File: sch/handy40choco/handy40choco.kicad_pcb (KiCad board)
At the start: 2 copper layers, 169 x 71 mm, 95 parts, among them J1 Conn_01x20, SW1 SW_Push, SW10 SW_Push, SW11 SW_Push, SW12 SW_Push, SW13 SW_Push, SW14 SW_Push, SW15 SW_Push, SW16 SW_Push, SW17 SW_Push, SW18 SW_Push, SW19 SW_Push, SW2 SW_Push, SW20 SW_Push, SW21 SW_Push, SW22 SW_Push, SW23 SW_Push, SW24 SW_Push, SW25 SW_Push, SW26 SW_Push, SW27 SW_Push, SW28 SW_Push, SW29 SW_Push, SW3 SW_Push, SW30 SW_Push, SW31 SW_Push, SW32 SW_Push, SW33 SW_Push, SW34 SW_Push, SW35 SW_Push, SW36 SW_Push, SW37 SW_Push, SW38 SW_Push, SW39 SW_Push, SW4 SW_Push, SW40 SW_Push, SW5 SW_Push, SW6 SW_Push, SW7 SW_Push, SW8 SW_Push, SW9 SW_Push

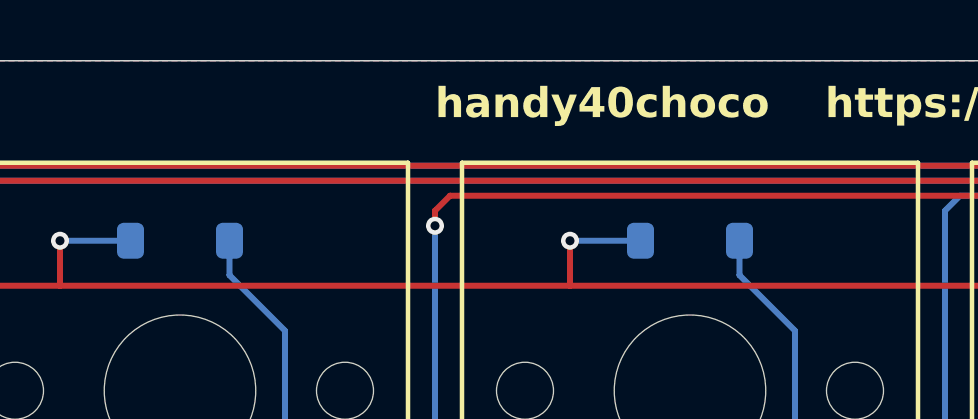
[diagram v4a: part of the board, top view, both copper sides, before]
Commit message: マイコン基板(pico)の雛形です。
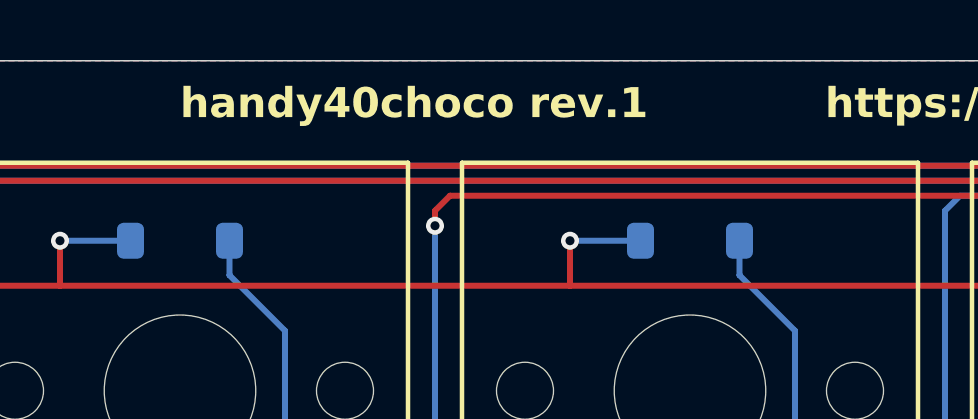
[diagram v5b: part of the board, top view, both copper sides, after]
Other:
- board text added: "handy40choco rev.1"
- board text removed: "handy40choco"
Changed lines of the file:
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@@
 		)
 	)
-	(gr_text "handy40choco"
-		(at 108.5 88 0)
+	(gr_text "handy40choco rev.1"
+		(at 100 88 0)
 		(layer "F.SilkS")
 		(effects
